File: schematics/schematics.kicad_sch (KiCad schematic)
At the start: 5 parts, among them U1 Pico, U2 BME680, U3 AHT20

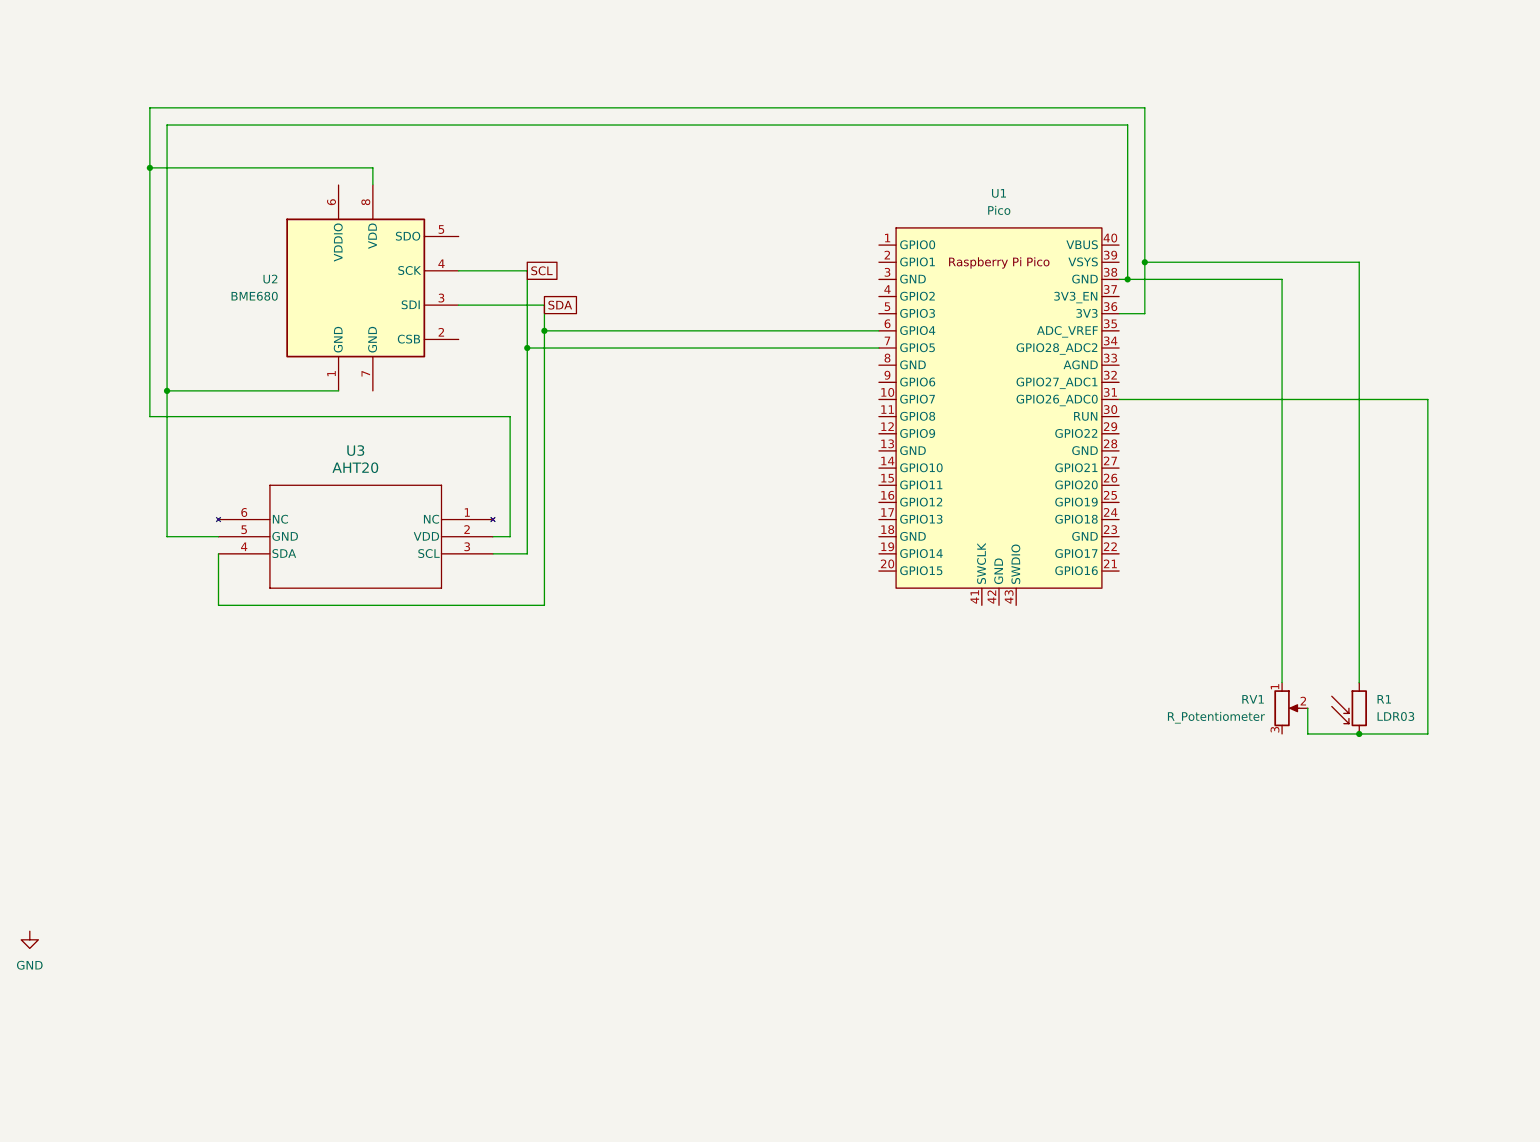
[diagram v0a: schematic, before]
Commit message: Fixed BME680 bug
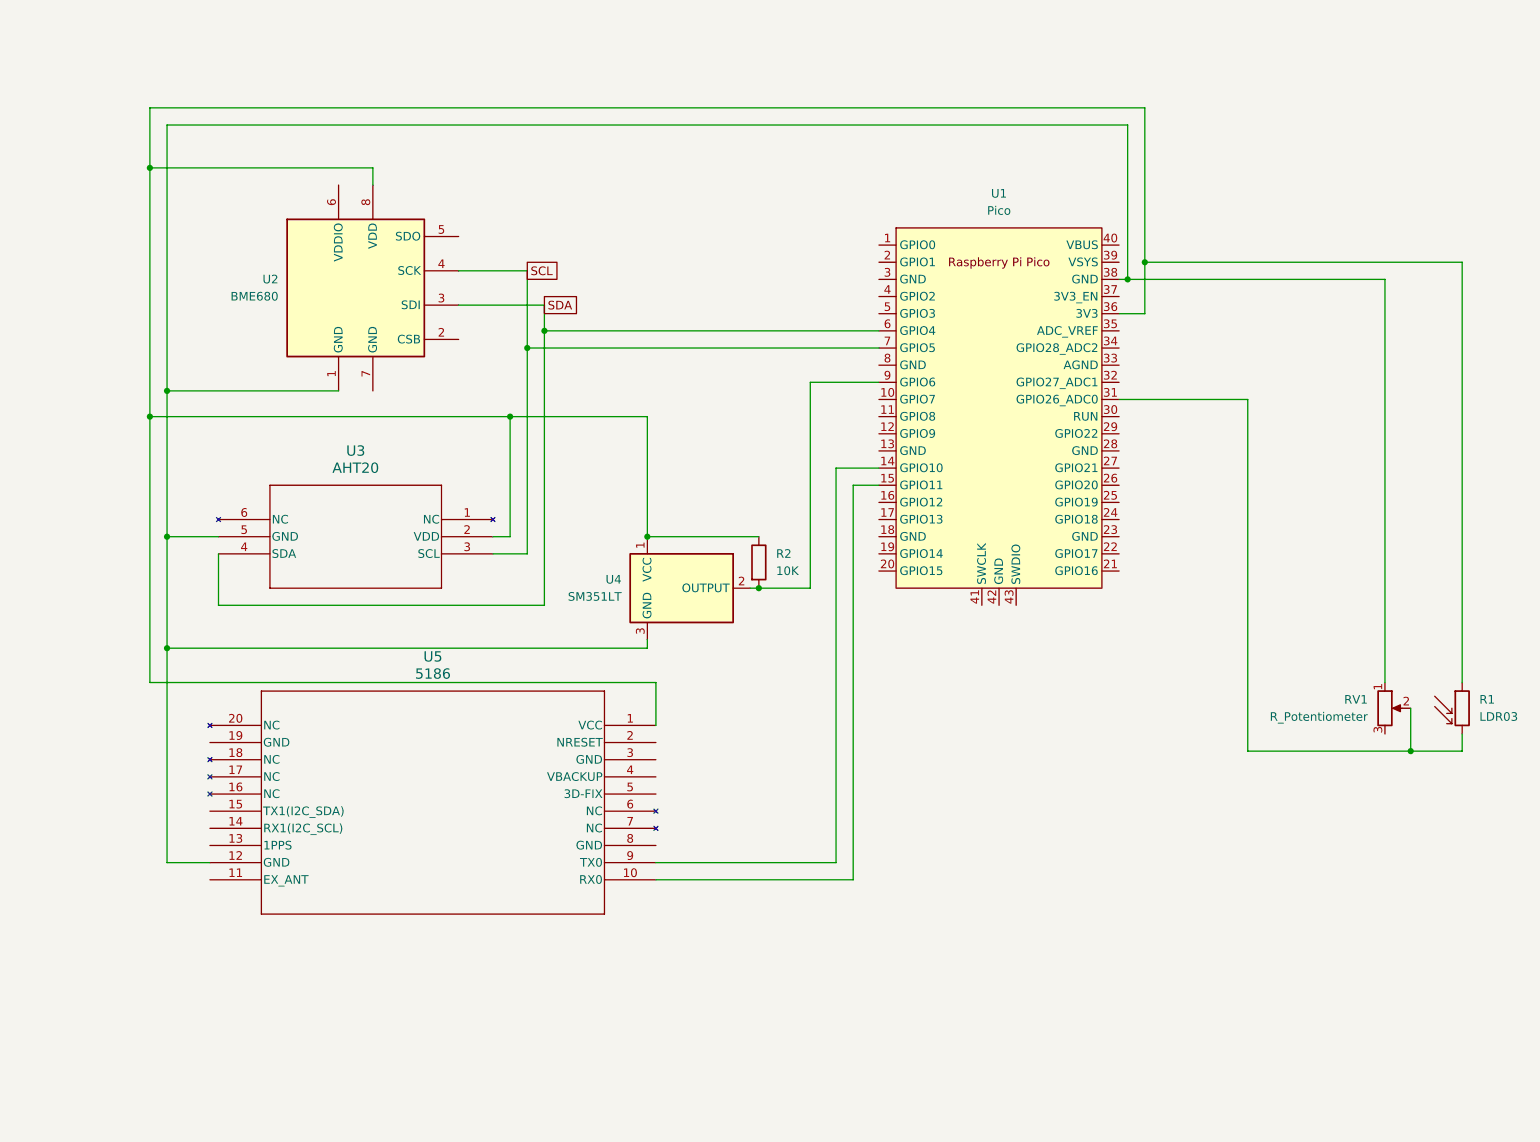
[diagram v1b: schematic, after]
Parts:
- added R2: 10K, symbol Device:R
- added U4: SM351LT, Package_TO_SOT_SMD:SOT-23, symbol Sensor_Magnetic:SM351LT
- added U5: 5186, CD-PA1616D_ADA, symbol PA1616D:5186
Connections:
- net at R1.1, U1.36 (3V3), U2.8 (VDD)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: now also R2.1, U4.1 (VCC), U5.1 (VCC)
- net at RV1.1, U1.38 (GND), U2.1 (GND)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: now also U4.3 (GND), U5.12 (GND)
- net at U1.14 (GPIO10): now also U5.9 (TX0)
- net at U1.15 (GPIO11): now also U5.10 (RX0)
- net at U1.9 (GPIO6): now also R2.2, U4.2 (OUTPUT)
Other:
- moved on the sheet: R1, RV1

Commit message: Finished schematics, fixed potential task priority issue
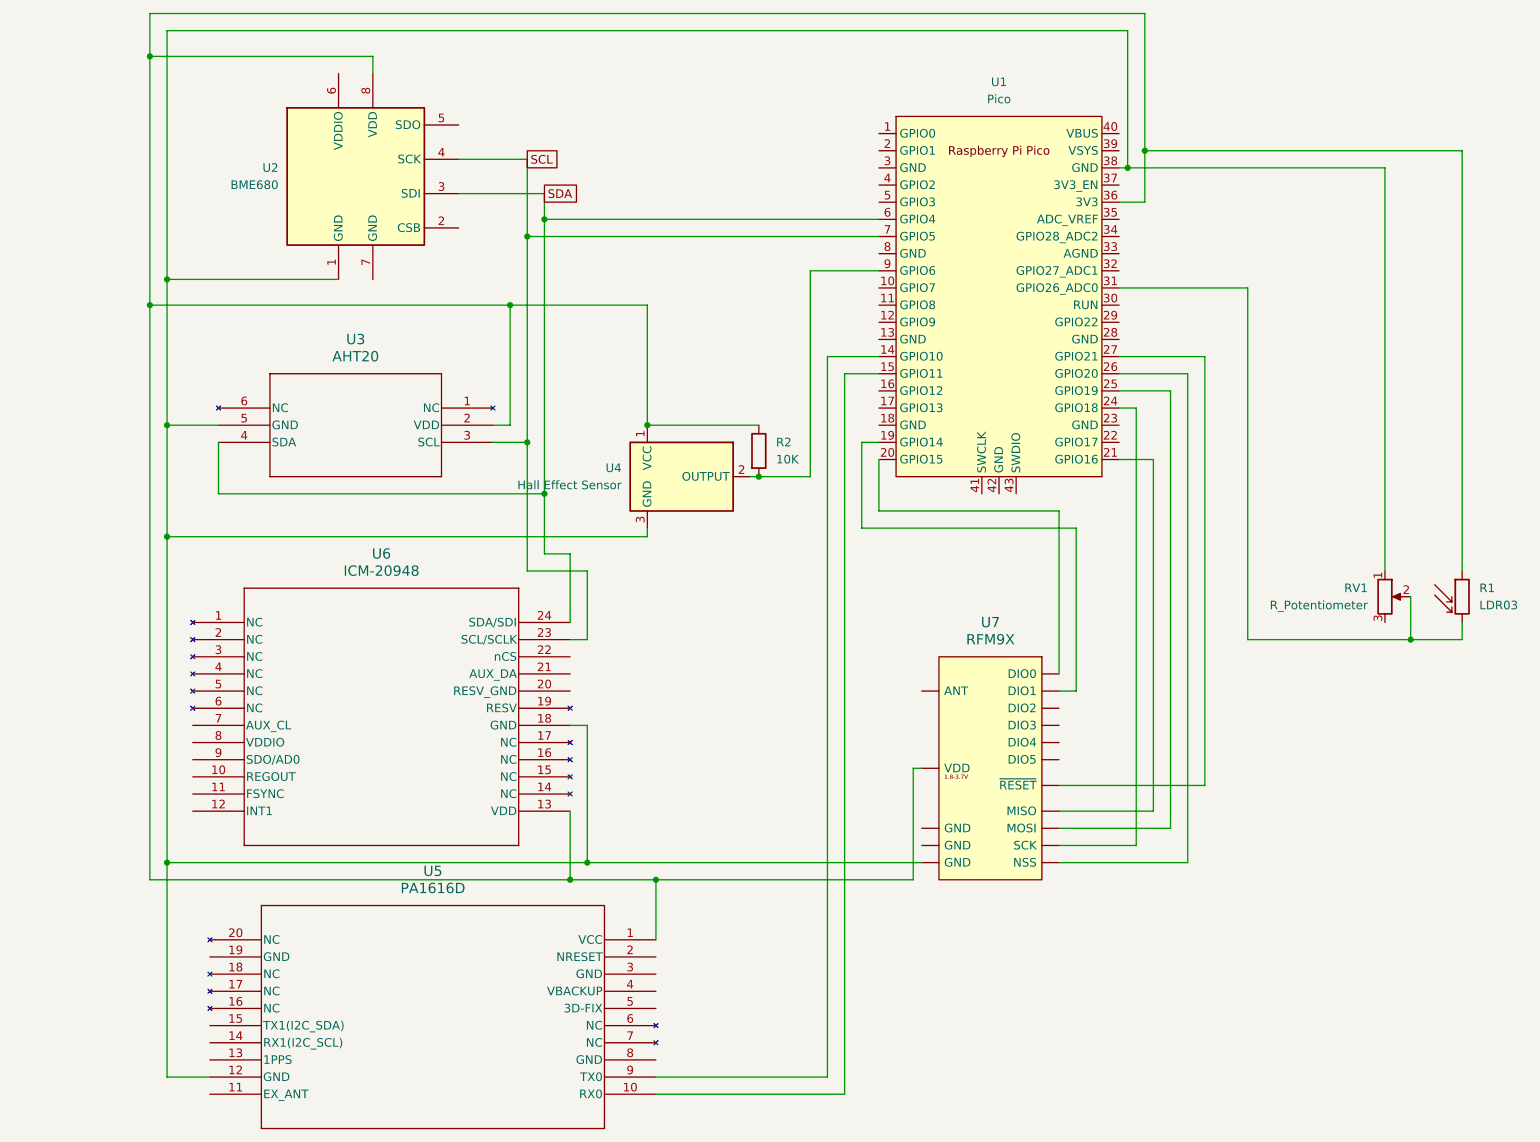
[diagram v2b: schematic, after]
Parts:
- added U6: ICM-20948, QFN24_3X3X0P9_IVS, symbol ICM-20948:ICM-20948
- added U7: RFM9X, symbol RFM9X:RFM9X
- U4: value SM351LT -> Hall Effect Sensor
- U5: value 5186 -> PA1616D
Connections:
- net SCL: now also U6.23 (SCL/SCLK)
- net SDA: now also U6.24 (SDA/SDI)
- net at R1.1, R2.1, U1.36 (3V3)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: now also U6.13 (VDD), U7.12 (VDD)
- net at RV1.1, U1.38 (GND), U2.1 (GND)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: now also U6.18 (GND), U7.15 (GND)
- net at U1.19 (GPIO14): now also U7.10 (DIO1)
- net at U1.20 (GPIO15): now also U7.11 (DIO0)
- net at U1.21 (GPIO16): now also U7.2 (MISO)
- net at U1.24 (GPIO18): now also U7.4 (SCK)
- net at U1.25 (GPIO19): now also U7.3 (MOSI)
- net at U1.26 (GPIO20): now also U7.5 (NSS)
- net at U1.27 (GPIO21): now also U7.6 (~{RESET})
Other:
- moved on the sheet: R1, R2, RV1, U1, U2, U3, U4, U5

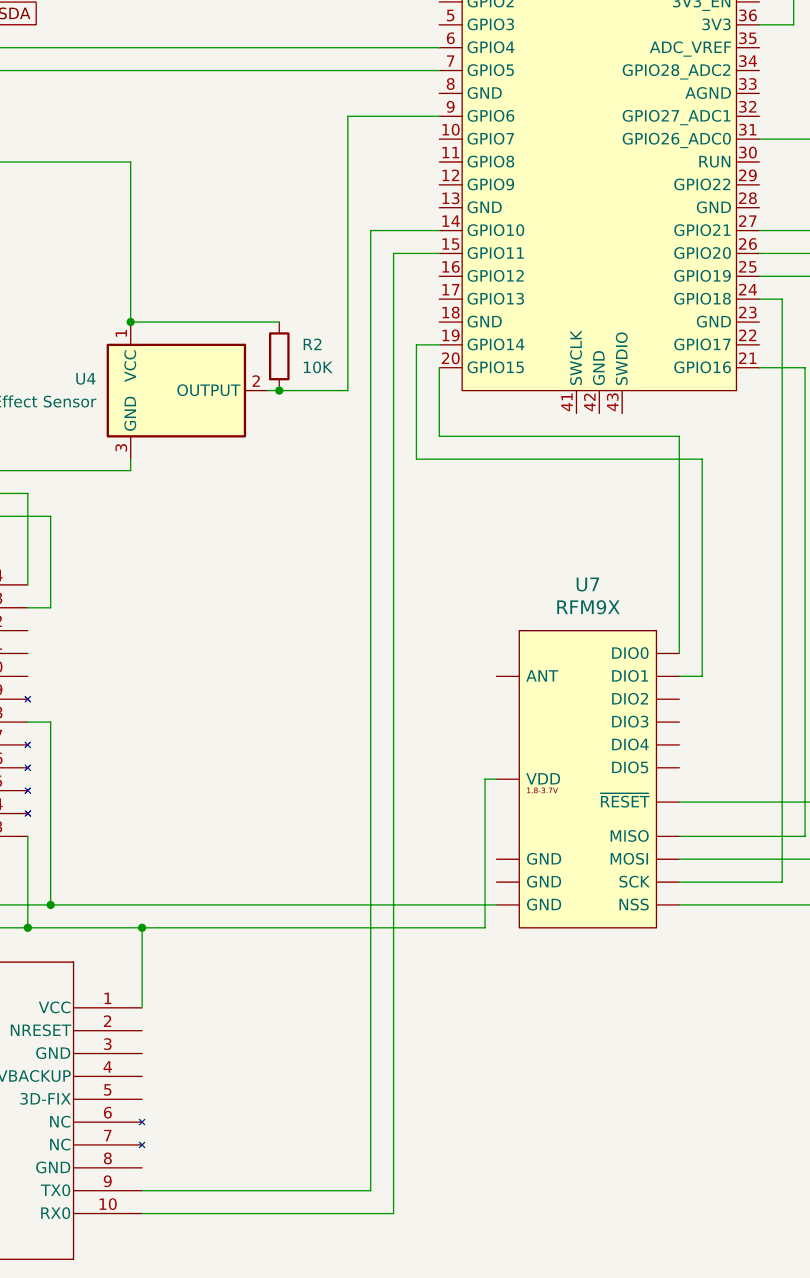
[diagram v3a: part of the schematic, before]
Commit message: Added semaphore to tPrintf function
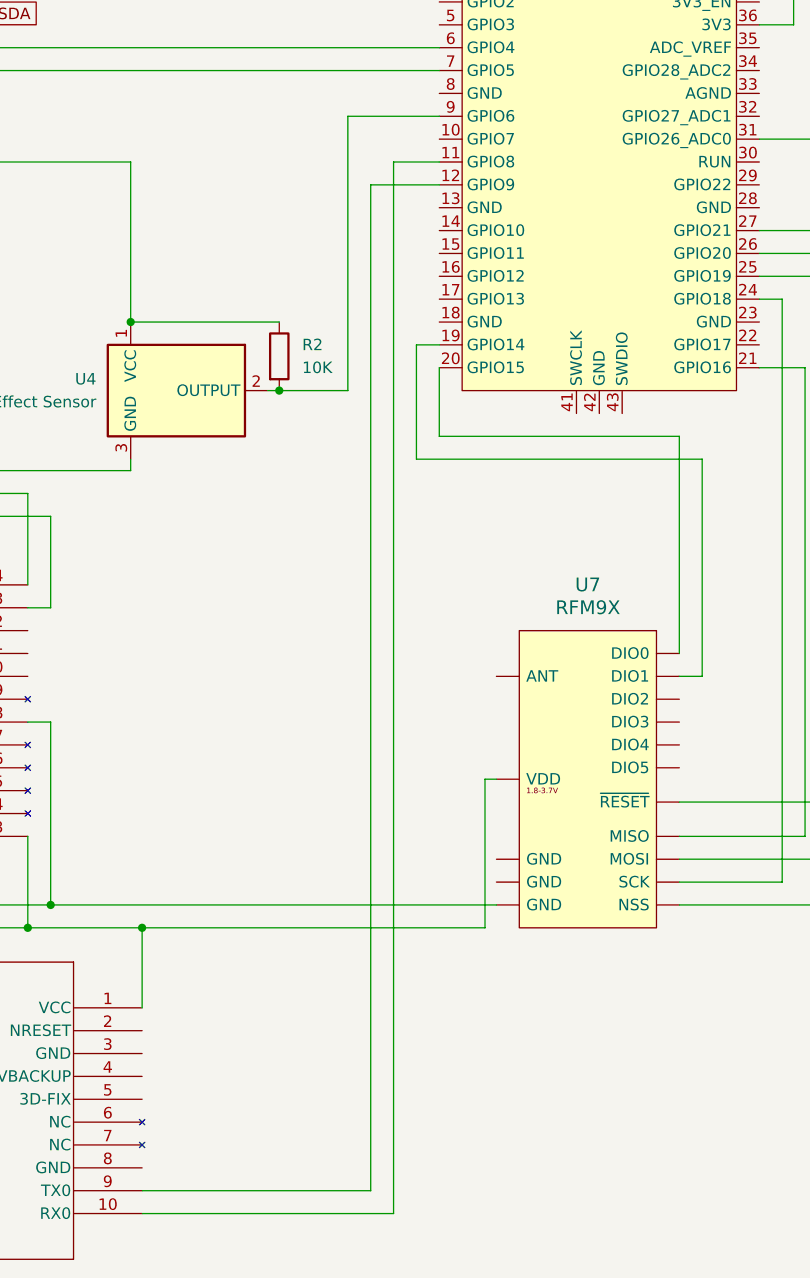
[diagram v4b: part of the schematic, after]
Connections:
- net at U1.11 (GPIO8): now also U5.10 (RX0)
- net at U1.12 (GPIO9): now also U5.9 (TX0)
- net at U1.14 (GPIO10): no longer U5.9 (TX0)
- net at U1.15 (GPIO11): no longer U5.10 (RX0)
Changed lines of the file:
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@@
+	(wire
+		(pts
+			(xy 151.13 62.23) (xy 156.21 62.23)
+		)
+		(stroke
+			(width 0)
+			(type default)
+		)
+	)
 	(wire
 		(pts
@@
 	(wire
 		(pts
-			(xy 148.59 69.85) (xy 156.21 69.85)
+			(xy 148.59 176.53) (xy 148.59 64.77)
 		)
 		(stroke
@@
 	(wire
 		(pts
-			(xy 148.59 69.85) (xy 148.59 176.53)
-		)
-		(stroke
-			(width 0)
-			(type default)
-		)
-	)
-	(wire
-		(pts
 			(xy 48.26 62.23) (xy 101.6 62.23)
 		)
@@
 	(wire
 		(pts
+			(xy 148.59 64.77) (xy 156.21 64.77)
+		)
+		(stroke
+			(width 0)
+			(type default)
+		)
+	)
+	(wire
+		(pts
 			(xy 50.8 58.42) (xy 76.2 58.42)
 		)
@@
 	(wire
 		(pts
-			(xy 151.13 72.39) (xy 151.13 179.07)
-		)
-		(stroke
-			(width 0)
-			(type default)
-		)
-	)
-	(wire
-		(pts
 			(xy 234.95 111.76) (xy 210.82 111.76)
 		)
@@
 	(wire
 		(pts
+			(xy 151.13 62.23) (xy 151.13 179.07)
+		)
+		(stroke
+			(width 0)
+			(type default)
+		)
+	)
+	(wire
+		(pts
 			(xy 162.56 144.78) (xy 113.03 144.78)
 		)
@@
 		)
 		(stroke
-			(width 0)
-			(type default)
-		)
-	)
-	(wire
-		(pts
-			(xy 151.13 72.39) (xy 156.21 72.39)
-		)
-		(stroke
